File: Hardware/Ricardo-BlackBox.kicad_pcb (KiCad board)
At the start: 4 copper layers, 45.1 x 35.1 mm, 83 parts, among them J1 RBUS, J2 USB_C_Receptacle_USB2.0, J3 Conn_01x08_Pin, U1 ESP32-S3, U2 SN65HVD230, U3 LM66200DRLR, U4 MAX77827AEFD+T, U5 SC4215ASTRT, U7 LM66200DRLR, Y1 R940000171

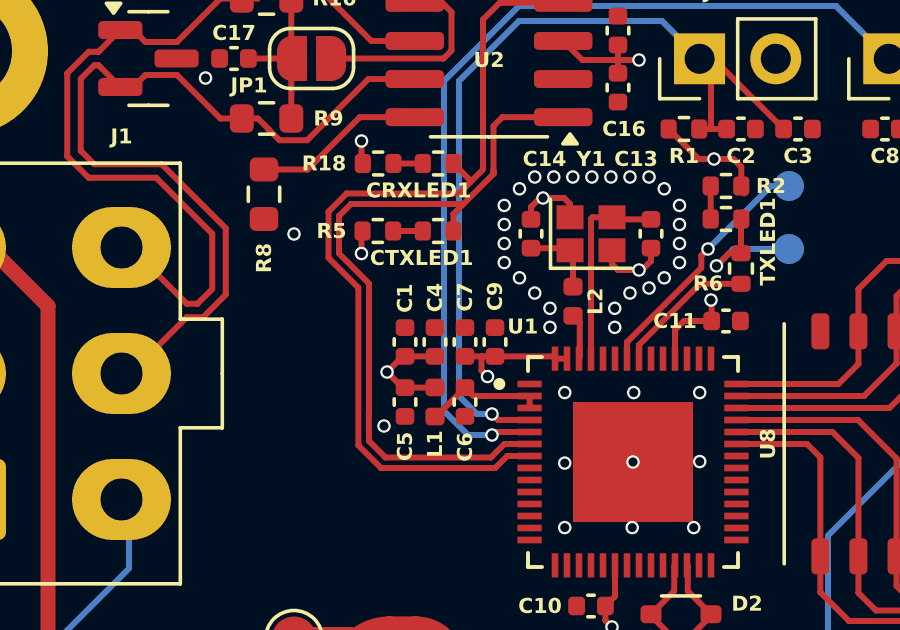
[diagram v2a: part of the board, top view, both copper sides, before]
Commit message: Added additional vias
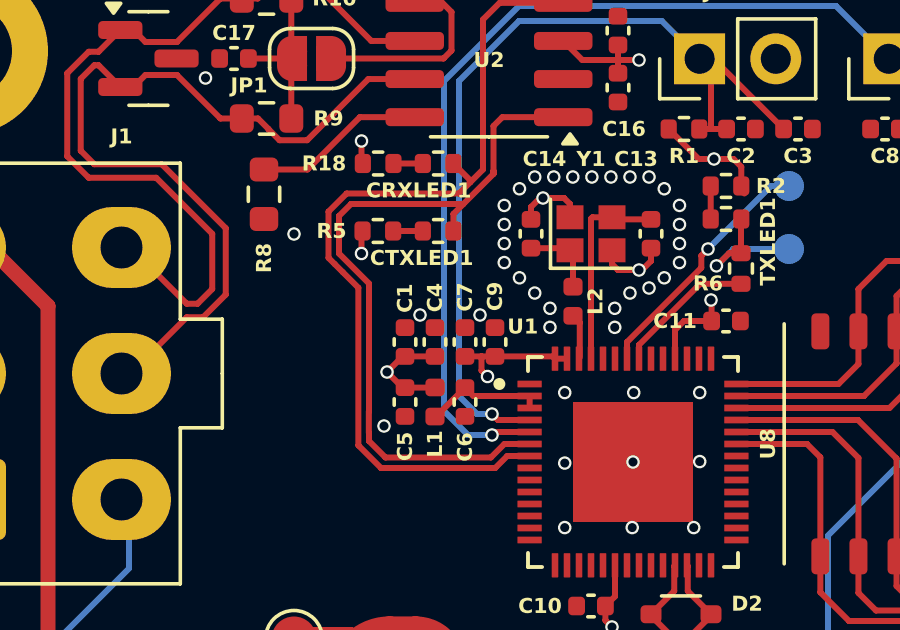
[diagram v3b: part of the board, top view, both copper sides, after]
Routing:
- net GND: vias 51 -> 53
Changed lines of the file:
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@@
 	)
 	(via
+		(at 97.625 57.89)
+		(size 0.45)
+		(drill 0.3)
+		(layers "F.Cu" "B.Cu")
+		(free yes)
+		(net 1)
+	)
+	(via
 		(at 101.725 53.99)
 		(size 0.45)
@@
 	)
 	(via
+		(at 99.625 57.89)
+		(size 0.45)
+		(drill 0.3)
+		(layers "F.Cu" "B.Cu")
+		(free yes)
+		(net 1)
+	)
+	(via
 		(at 106.275 55.5075)
 		(size 0.45)
@@
 	)
 	(zone
-		(net 3)
-		(net_name "VBUS")
-		(layer "F.Cu")
-		(name "$teardrop_padvia$")
-		(hatch full 0.1)
-		(priority 30000)
-		(attr
-			(teardrop
-				(type padvia)
-			)
-		)
-		(connect_pads yes
-			(clearance 0)
-		)
-		(min_thickness 0.0254)
-		(filled_areas_thickness no)
-		(fill yes
-			(thermal_gap 0.5)
-			(thermal_bridge_width 0.5)
-			(island_removal_mode 1)
-			(island_area_min 10)
-		)
-		(polygon
-			(pts
-				(xy 88.322458 76.138882) (xy 88.322458 75.888882) (xy 87.992992 75.694009) (xy 87.905888 75.901882)
-				(xy 87.906888 76.126882)
-			)
-		)
-	)
-	(zone
 		(net 5)
 		(net_name "/Power/BBIN")
@@
 	)
 	(zone
+		(net 1)
+		(net_name "GND")
+		(layer "F.Cu")
+		(name "$teardrop_padvia$")
+		(hatch full 0.1)
+		(priority 30001)
+		(attr
+			(teardrop
+				(type padvia)
+			)
+		)
+		(connect_pads yes
+			(clearance 0)
+		)
+		(min_thickness 0.0254)
+		(filled_areas_thickness no)
+		(fill yes
+			(thermal_gap 0.5)
+			(thermal_bridge_width 0.5)
+			(island_removal_mode 1)
+			(island_area_min 10)
+		)
+		(polygon
+			(pts
+				(xy 88.316888 72.386882) (xy 88.566888 72.386882) (xy 88.649761 72.022986) (xy 88.441888 71.935882)
+				(xy 88.234015 72.022986)
+			)
+		)
+	)
+	(zone
+		(net 1)
+		(net_name "GND")
+		(layer "F.Cu")
+		(name "$teardrop_padvia$")
+		(hatch full 0.1)
+		(priority 30003)
+		(attr
+			(teardrop
+				(type padvia)
+			)
+		)
+		(connect_pads yes
+			(clearance 0)
+		)
+		(min_thickness 0.0254)
+		(filled_areas_thickness no)
+		(fill yes
+			(thermal_gap 0.5)
+			(thermal_bridge_width 0.5)
+			(island_removal_mode 1)
+			(island_area_min 10)
+		)
+		(polygon
+			(pts
+				(xy 97.053482 69.861882) (xy 97.053482 69.661882) (xy 96.645784 69.864009) (xy 96.730888 70.071882)
+				(xy 96.939761 70.157986)
+			)
+		)
+	)
+	(zone
 		(net 9)
 		(net_name "/Power/LX2")
@@
 	)
 	(zone
-		(net 3)
-		(net_name "VBUS")
+		(net 1)
+		(net_name "GND")
 		(layer "F.Cu")
-		(name "$teardrop_padvia$")
-		(hatch full 0.1)
-		(priority 30002)
-		(attr
-			(teardrop
-				(type padvia)
-			)
-		)
+		(hatch edge 0.5)
+		(priority 1)
 		(connect_pads yes
 			(clearance 0)
 		)
-		(min_thickness 0.0254)
+		(min_thickness 0.25)
 		(filled_areas_thickness no)
 		(fill yes
 			(thermal_gap 0.5)
 			(thermal_bridge_width 0.5)
-			(island_removal_mode 1)
-			(island_area_min 10)
 		)
 		(polygon
 			(pts
-				(xy 87.316888 72.236441) (xy 87.566888 72.236441) (xy 87.843071 72.045814) (xy 87.683972 71.885715)
-				(xy 87.476099 71.800611)
+				(xy 128.425 83.09) (xy 73.425 83.09) (xy 73.425 43.09) (xy 128.425 43.09)
 			)
 		)
 	)
 	(zone
-		(net 1)
-		(net_name "GND")
+		(net 3)
+		(net_name "VBUS")
 		(layer "F.Cu")
-		(hatch edge 0.5)
-		(priority 1)
+		(name "$teardrop_padvia$")
+		(hatch full 0.1)
+		(priority 30000)
+		(attr
+			(teardrop
+				(type padvia)
+			)
+		)
 		(connect_pads yes
 			(clearance 0)
 		)
-		(min_thickness 0.25)
+		(min_thickness 0.0254)
 		(filled_areas_thickness no)
 		(fill yes
 			(thermal_gap 0.5)
 			(thermal_bridge_width 0.5)
+			(island_removal_mode 1)
+			(island_area_min 10)
 		)
 		(polygon
 			(pts
-				(xy 128.425 83.09) (xy 73.425 83.09) (xy 73.425 43.09) (xy 128.425 43.09)
+				(xy 88.322458 76.138882) (xy 88.322458 75.888882) (xy 87.992992 75.694009) (xy 87.905888 75.901882)
+				(xy 87.906888 76.126882)
 			)
 		)
@@
 	)
 	(zone
-		(net 1)
-		(net_name "GND")
-		(layer "F.Cu")
-		(name "$teardrop_padvia$")
-		(hatch full 0.1)
-		(priority 30001)
-		(attr
-			(teardrop
-				(type padvia)
-			)
-		)
-		(connect_pads yes
-			(clearance 0)
-		)
-		(min_thickness 0.0254)
-		(filled_areas_thickness no)
-		(fill yes
-			(thermal_gap 0.5)
-			(thermal_bridge_width 0.5)
-			(island_removal_mode 1)
-			(island_area_min 10)
-		)
-		(polygon
-			(pts
-				(xy 88.316888 72.386882) (xy 88.566888 72.386882) (xy 88.649761 72.022986) (xy 88.441888 71.935882)
-				(xy 88.234015 72.022986)
-			)
-		)
-	)
-	(zone
-		(net 1)
-		(net_name "GND")
+		(net 3)
+		(net_name "VBUS")
 		(layer "F.Cu")
 		(name "$teardrop_padvia$")
 		(hatch full 0.1)
-		(priority 30003)
+		(priority 30002)
 		(attr
 			(teardrop
@@
 		(polygon
 			(pts
-				(xy 97.053482 69.861882) (xy 97.053482 69.661882) (xy 96.645784 69.864009) (xy 96.730888 70.071882)
-				(xy 96.939761 70.157986)
+				(xy 87.316888 72.236441) (xy 87.566888 72.236441) (xy 87.843071 72.045814) (xy 87.683972 71.885715)
+				(xy 87.476099 71.800611)
 			)
 		)
@@
 		(name "$teardrop_padvia$")
 		(hatch full 0.1)
-		(priority 30000)
+		(priority 30001)
 		(attr
 			(teardrop
@@
 		(polygon
 			(pts
-				(xy 88.090558 71.656906) (xy 87.913781 71.480129) (xy 87.597868 71.678842) (xy 87.683265 71.887422)
-				(xy 87.891845 71.972819)
+				(xy 88.026888 75.452877) (xy 87.776888 75.452877) (xy 87.699015 75.815778) (xy 87.906888 75.902882)
+				(xy 88.114761 75.815778)
 			)
 		)
 	)
 	(zone
-		(net 1)
-		(net_name "GND")
+		(net 3)
+		(net_name "VBUS")
 		(layer "B.Cu")
-		(hatch edge 0.5)
-		(priority 1)
+		(name "$teardrop_padvia$")
+		(hatch full 0.1)
+		(priority 30000)
+		(attr
+			(teardrop
+				(type padvia)
+			)
+		)
 		(connect_pads yes
 			(clearance 0)
 		)
-		(min_thickness 0.25)
+		(min_thickness 0.0254)
 		(filled_areas_thickness no)
 		(fill yes
 			(thermal_gap 0.5)
 			(thermal_bridge_width 0.5)
+			(island_removal_mode 1)
+			(island_area_min 10)
 		)
 		(polygon
 			(pts
-				(xy 135.925 35.59) (xy 135.925 90.59) (xy 65.925 90.59) (xy 65.925 35.59)
+				(xy 88.090558 71.656906) (xy 87.913781 71.480129) (xy 87.597868 71.678842) (xy 87.683265 71.887422)
+				(xy 87.891845 71.972819)
 			)
 		)
 	)
 	(zone
-		(net 3)
-		(net_name "VBUS")
+		(net 1)
+		(net_name "GND")
 		(layer "B.Cu")
-		(name "$teardrop_padvia$")
-		(hatch full 0.1)
-		(priority 30001)
-		(attr
-			(teardrop
-				(type padvia)
-			)
-		)
+		(hatch edge 0.5)
+		(priority 1)
 		(connect_pads yes
 			(clearance 0)
 		)
-		(min_thickness 0.0254)
+		(min_thickness 0.25)
 		(filled_areas_thickness no)
 		(fill yes
 			(thermal_gap 0.5)
 			(thermal_bridge_width 0.5)
-			(island_removal_mode 1)
-			(island_area_min 10)
 		)
 		(polygon
 			(pts
-				(xy 88.026888 75.452877) (xy 87.776888 75.452877) (xy 87.699015 75.815778) (xy 87.906888 75.902882)
-				(xy 88.114761 75.815778)
+				(xy 135.925 35.59) (xy 135.925 90.59) (xy 65.925 90.59) (xy 65.925 35.59)
 			)
 		)

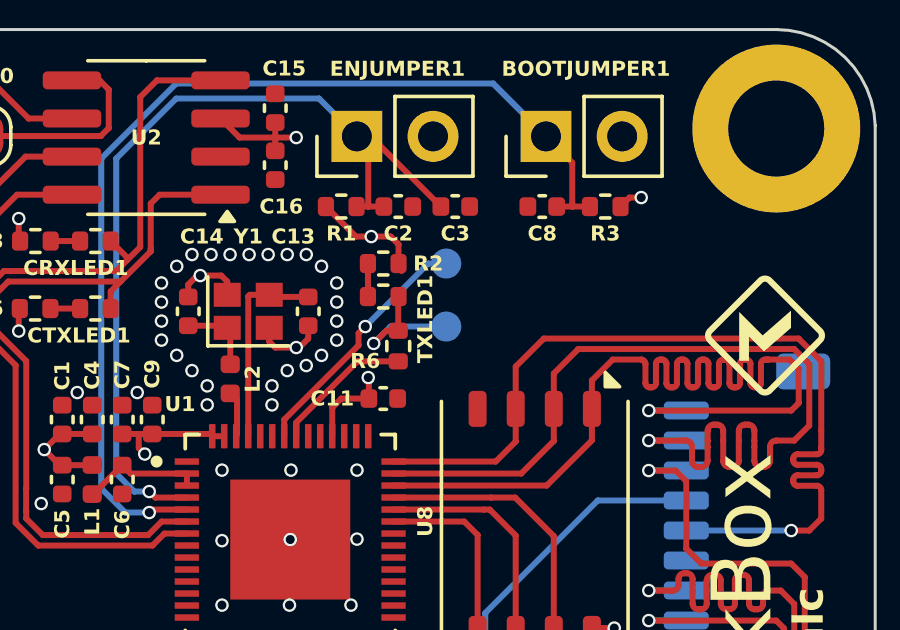
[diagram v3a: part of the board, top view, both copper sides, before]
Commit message: Move TXD/RXD pads
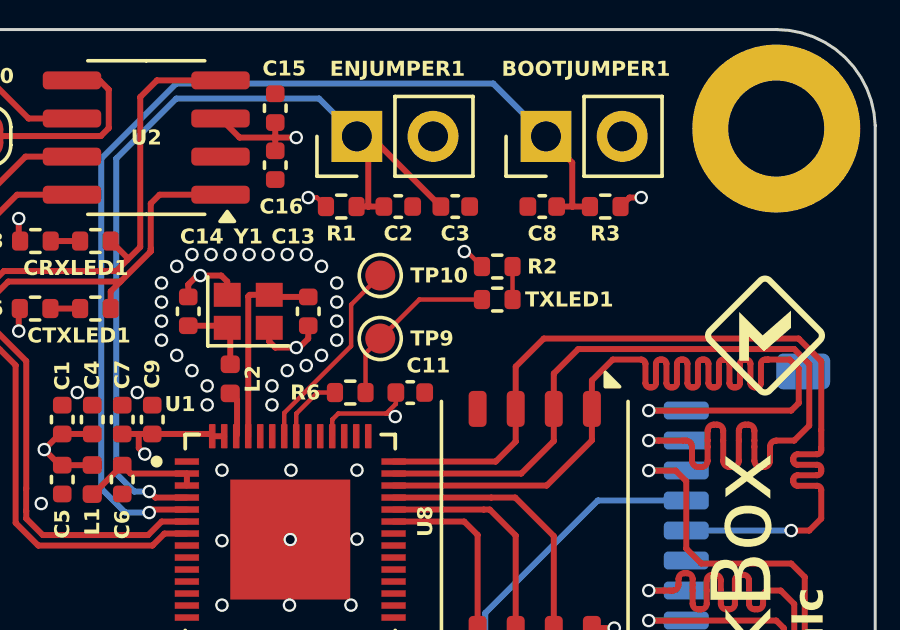
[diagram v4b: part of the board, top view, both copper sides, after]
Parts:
- TP10, TP9: moved to F.Cu
- moved R2 3.80 mm to (111.6, 53.7), turned to 0 degrees
- moved TXLED1 3.80 mm to (111.6, 54.8), turned to 0 degrees
- moved TP9 2.24 mm to (107.7, 56.1), turned to 0 degrees
- moved TP10 2.24 mm to (107.7, 54.0), turned to 0 degrees
- moved R6 2.23 mm to (106.7, 57.9), turned to 180 degrees
- moved C11 0.92 mm to (108.7, 57.9)
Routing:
- net Net-(U1-U0TXD/PROG/GPIO43): track 4.70 -> 2.33 mm
- net /RXD: track 8.34 -> 6.68 mm, vias 1 -> 0
- net +3V3: track 29.9 -> 28.5 mm, vias 14 -> 15
- net /TXD: track 4.79 -> 5.95 mm, vias 1 -> 0

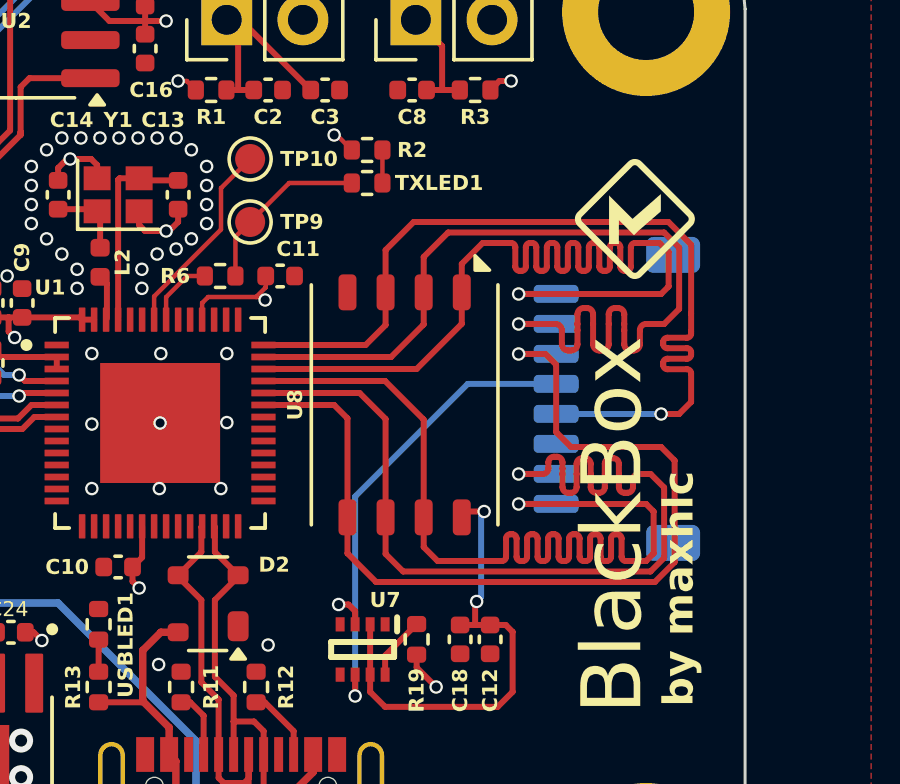
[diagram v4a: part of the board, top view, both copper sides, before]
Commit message: Move NAND flash chip
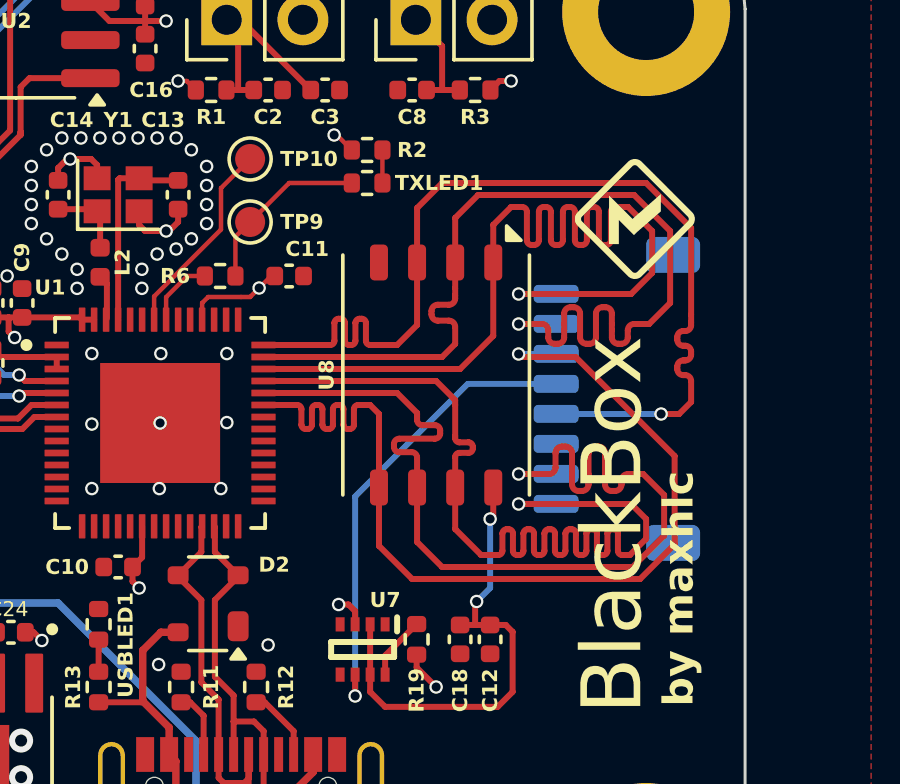
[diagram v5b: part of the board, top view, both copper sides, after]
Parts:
- moved U8 1.45 mm to (113.9, 61.2)
- moved C11 0.30 mm to (109.0, 57.9)
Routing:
- net /NAND_CLK: track 30.8 -> 33.9 mm
- net /NAND_CMD: track 31.7 -> 34.0 mm
- net /NAND_SD3: track 32.2 -> 33.9 mm
- net /NAND_SD0: track 33.1 -> 33.9 mm
- net /NAND_SD1: track 34.4 -> 33.9 mm

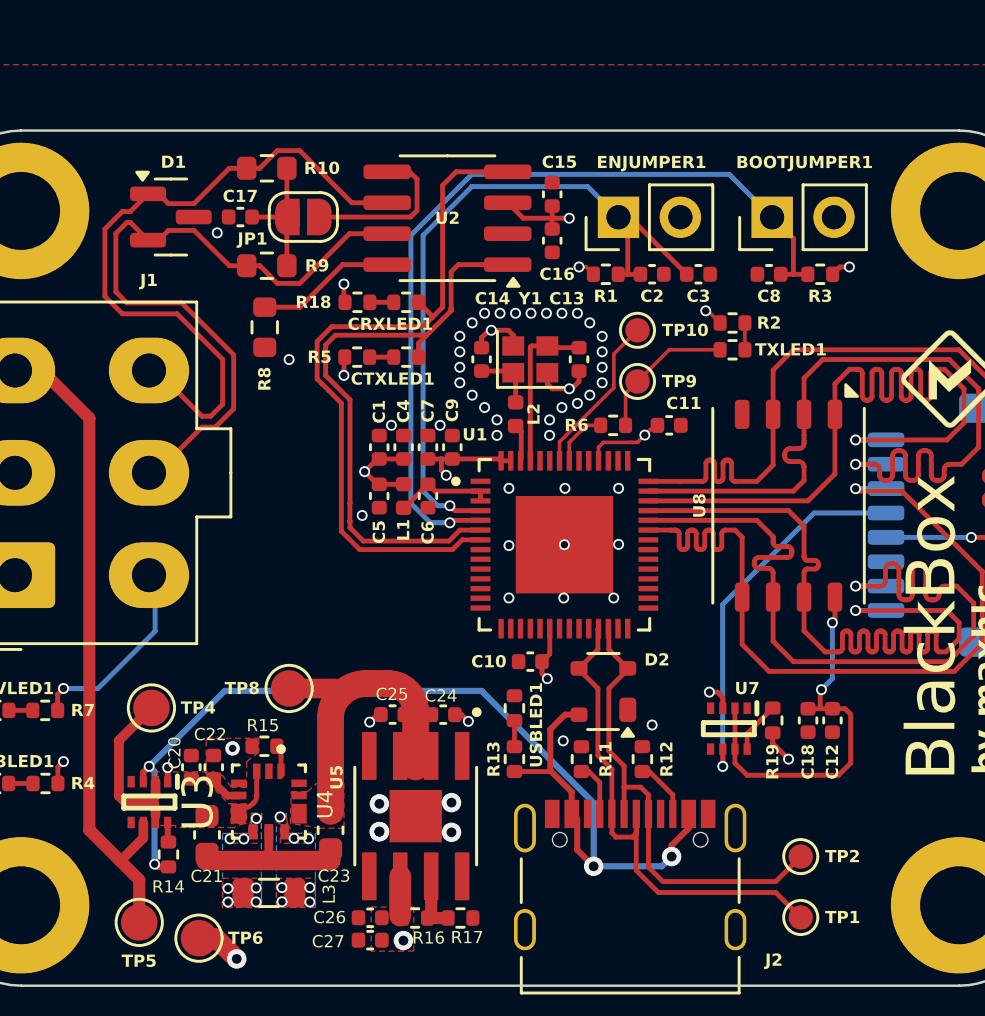
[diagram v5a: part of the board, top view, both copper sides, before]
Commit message: Ensure VBUS connections after ESD protection
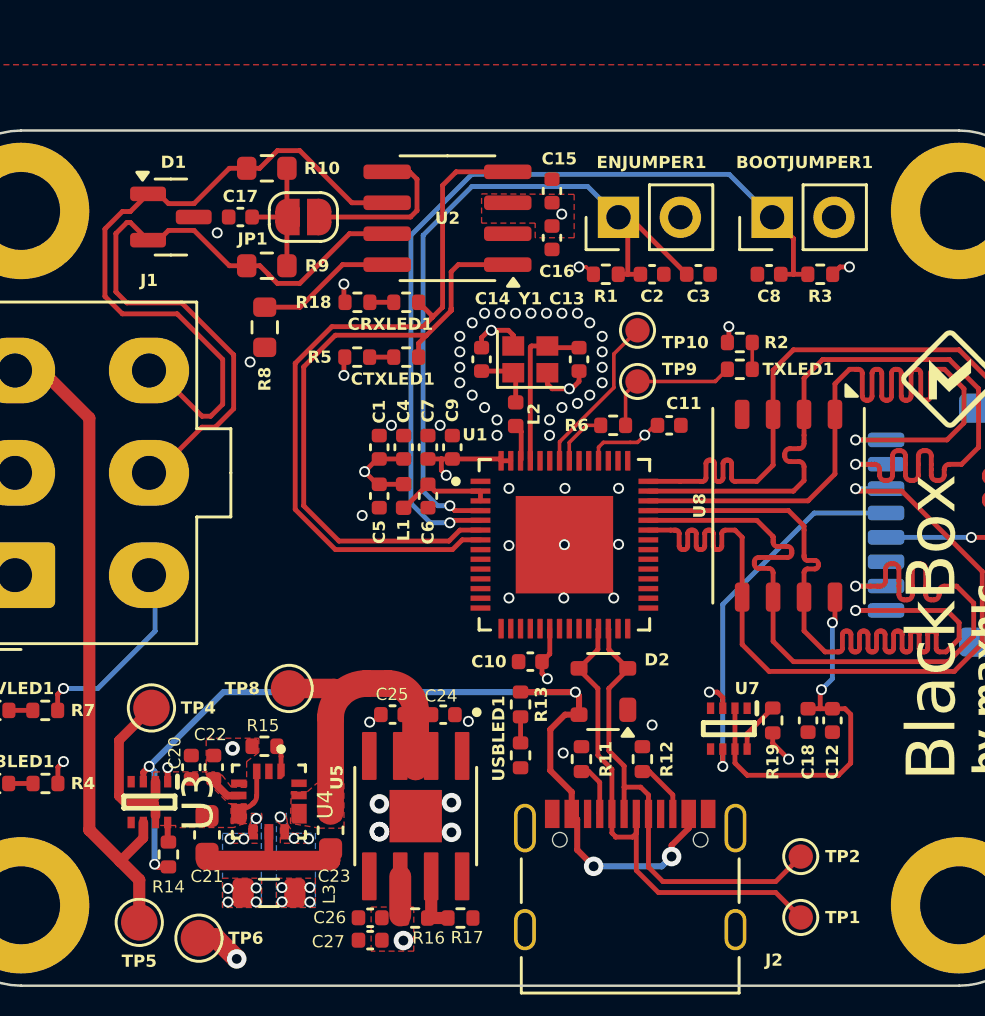
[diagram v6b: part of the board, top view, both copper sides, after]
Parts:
- moved R13 2.26 mm to (102.9, 69.3), turned to -90 degrees
- moved USBLED1 1.95 mm to (102.9, 71.4), turned to 90 degrees
- moved R2 0.85 mm to (111.9, 54.5)
- moved TXLED1 0.85 mm to (111.9, 55.6)
- moved C15 0.14 mm to (104.2, 48.3)
- moved C16 0.12 mm to (104.2, 50.2)
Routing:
- net +3V3: track 28.2 -> 24.3 mm
- net VBUS: track 44.3 -> 40.8 mm, vias 4 -> 5
- net /CAN_RX: track 29.2 -> 30.5 mm
- net /CAN_TX: track 24.6 -> 25.9 mm
- net GND: track 14.1 -> 13.0 mm
